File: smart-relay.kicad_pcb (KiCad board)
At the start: 2 copper layers, 16 parts, among them IC1 TMCS1101A4BQDR, J1 Screw_Terminal_01x03, J2 Conn_01x04, K1 G5LE-1, Q1 BSS138K, U1 OPAMP, U2 ATtiny85-20PU

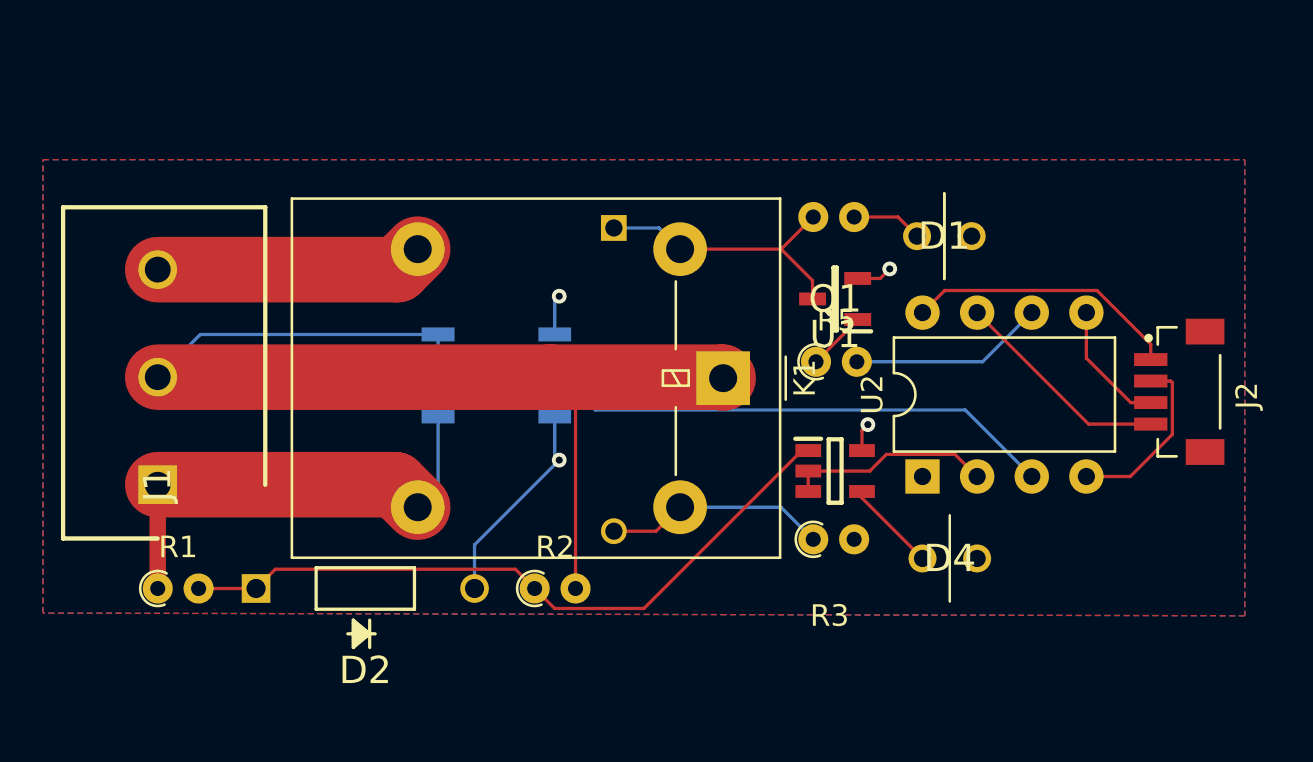
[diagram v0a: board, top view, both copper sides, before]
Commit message: add thicker traces
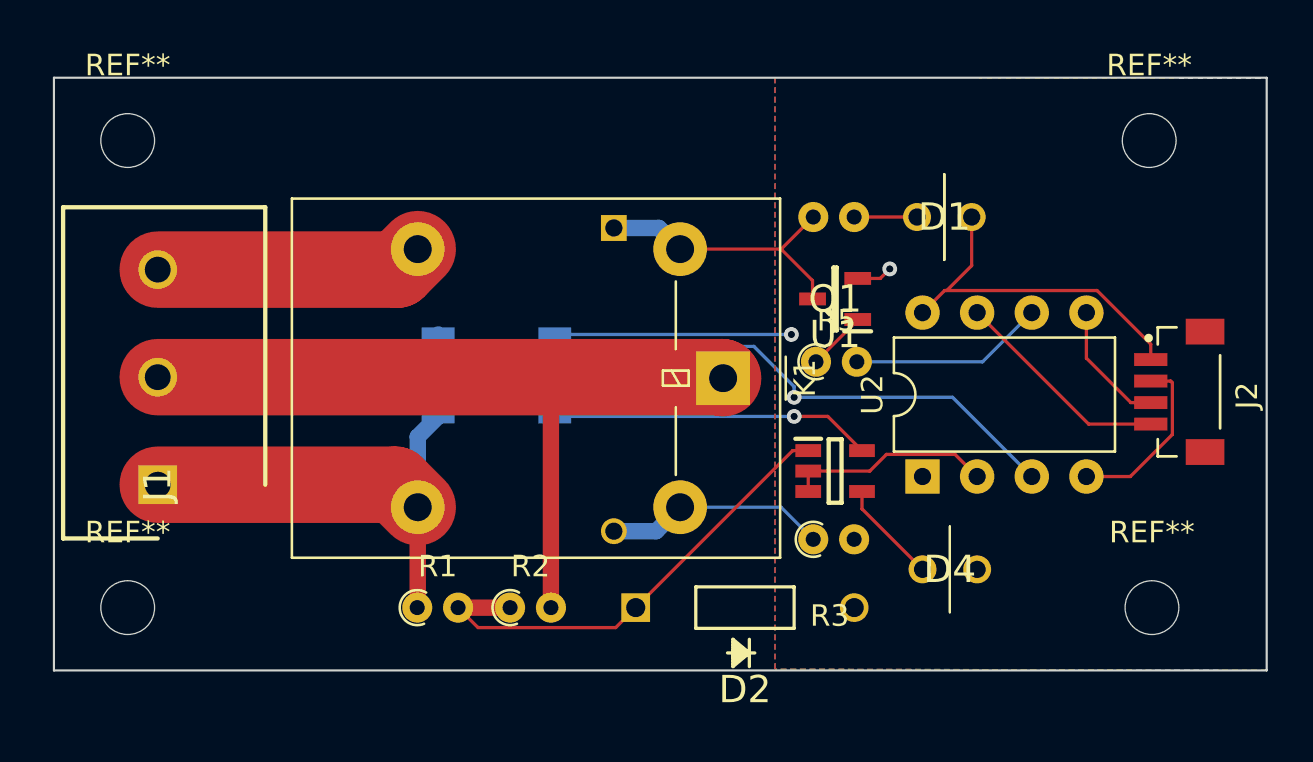
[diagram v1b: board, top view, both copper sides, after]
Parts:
- added REF**: MountingHole_2.5mm, MountingHole:MountingHole_2.5mm, F.Cu at (110.1, 69.1)
- added REF**: MountingHole_2.5mm, MountingHole:MountingHole_2.5mm, F.Cu at (110.0, 47.4)
- added REF**: MountingHole_2.5mm, MountingHole:MountingHole_2.5mm, F.Cu at (62.5, 69.1)
- added REF**: MountingHole_2.5mm, MountingHole:MountingHole_2.5mm, F.Cu at (62.5, 47.4)
- moved D2 17.7 mm to (86.1, 69.1)
- moved R1 12.1 mm to (75.9, 69.1)
- moved R2 1.45 mm to (80.3, 69.1)
- moved D1 0.89 mm to (99.2, 50.9)
- moved D4 0.51 mm to (99.4, 67.3)
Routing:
- net Net-(D2-Pad2): track 32.5 -> 22.5 mm
- net GND: track 16.1 -> 25.7 mm
- net +3V3: track 23.8 -> 31.6 mm, vias 2 -> 1
- net ISENSE: track 23.9 -> 25.8 mm, vias 0 -> 1
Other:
- board outline added: 56.4 x 27.6 mm
